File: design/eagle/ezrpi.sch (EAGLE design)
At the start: 40 parts

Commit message: unified cap value 100nF = 0.1uF
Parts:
- C9: value 100nF -> 0.1uF
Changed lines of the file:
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@@
 <part name="C7" library="passive" deviceset="CAP" device="0805" value="0.1uF"/>
 <part name="C8" library="passive" deviceset="CAP" device="0805" value="0.1uF"/>
-<part name="C9" library="passive" deviceset="CAP" device="0805" value="100nF"/>
+<part name="C9" library="passive" deviceset="CAP" device="0805" value="0.1uF"/>
 <part name="GND-ISO5" library="setup" deviceset="GND" device=""/>
 <part name="C10" library="passive" deviceset="CAP" device="0805" value="0.1uF"/>

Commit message: added top ground plane, fixed silk & naming
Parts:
- removed U$3: JTAG-6PINS, setup:JTAG-6PINS
- removed U$4: 26MHz, xtal:ABM8
- added SMA: (no value), connector:SMACONNECTOR
- added SWD: FTSH2X5, connector:FTSH2X5
- X1: value (none) -> 26MHz; device connector:SMACONNECTOR -> xtal:ABM8
- renumbered U$1 to MCU, U$2 to RPI, U$5 to X3, U$6 to X2
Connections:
- net GND: now also SMA.GND1, SMA.GND2, SMA.GND3, SMA.GND4, SWD.GND@1, SWD.GND@2, SWD.GND@3, X1.GND@2, X1.GND@4; no longer U$3.GND, U$4.GND@2, U$4.GND@4, X1.GND1, X1.GND2, X1.GND3, X1.GND4
- net N$1: now also SMA.ANT; no longer X1.ANT
- net RESET: now also SWD.RESET; no longer U$3.RESET
- net SWCLK: now also SWD.SWCLK; no longer U$3.SWCLK
- net SWDIO: now also SWD.SWDIO; no longer U$3.SWDIO
- net SWO: now also SWD.SWO; no longer U$3.SWO
- net VCC: now also SWD.VCC; no longer U$3.VCC
- net XIN: now also X1.1; no longer U$4.1
- net XOUT: now also X1.3; no longer U$4.3

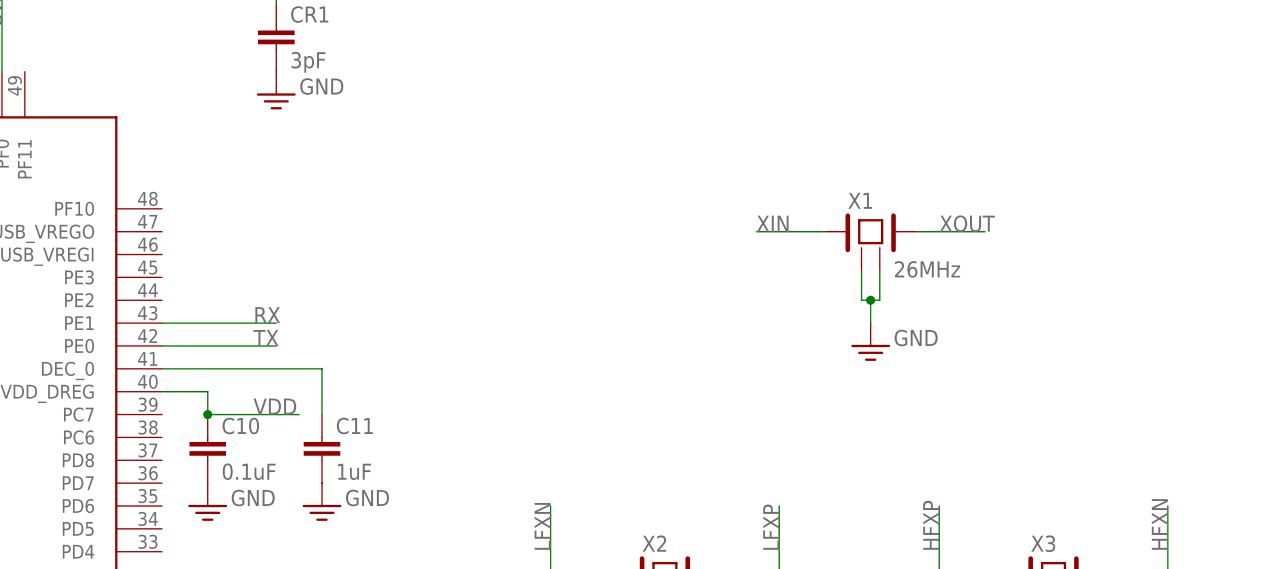
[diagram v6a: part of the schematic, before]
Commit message: added LEDs, improved traces, 50 Ω line, added vias
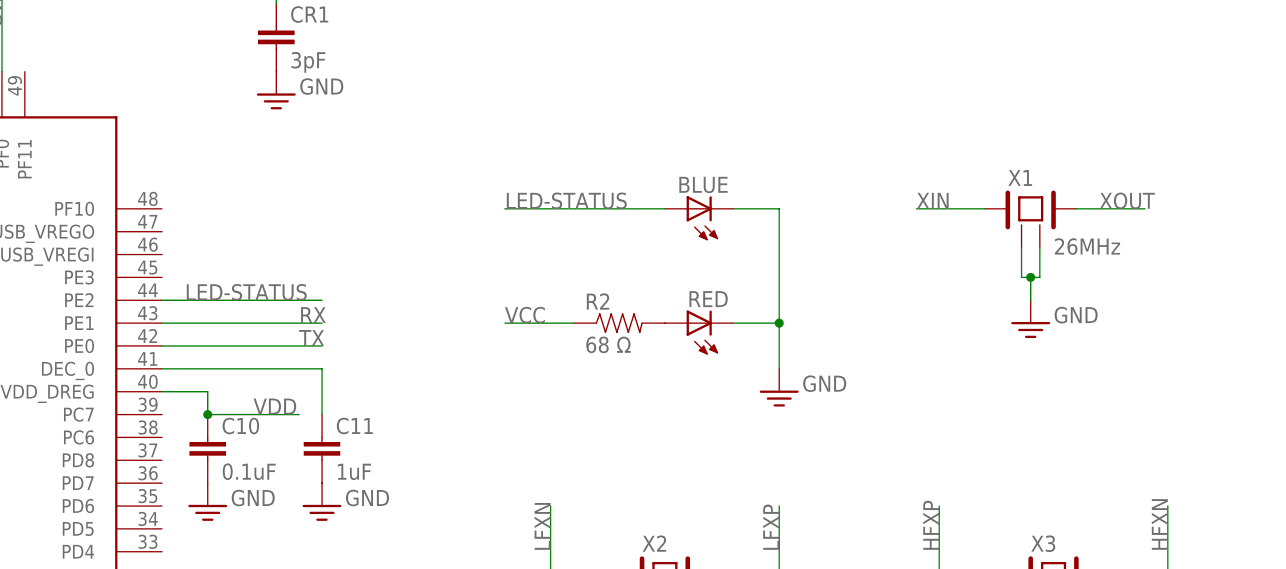
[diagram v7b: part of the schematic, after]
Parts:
- added BLUE, RED: (no value), led:LEDCHIPLED_0805
- added R2: 68 Ω, passive:RESISTOR0805-RES
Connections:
- new net LED-STATUS: BLUE.A, MCU.PE2
- new net N$8: R2.2, RED.A
- net GND: now also BLUE.C, RED.C
- net VCC: now also R2.1
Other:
- moved on the sheet: X1
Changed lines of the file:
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@@
 <part name="C0" library="passive" deviceset="CAP" device="0805" value="1uF"/>
 <part name="SWD" library="connector" deviceset="FTSH2X5" device=""/>
+<part name="BLUE" library="led" deviceset="LED" device="CHIPLED_0805"/>
+<part name="RED" library="led" deviceset="LED" device="CHIPLED_0805"/>
+<part name="R2" library="passive" deviceset="RESISTOR" device="0805-RES" value="68 Ω"/>
+<part name="GND" library="setup" deviceset="GND" device=""/>
 </parts>
 <sheets>
@@
 <instance part="GND-ISO17" gate="G$1" x="251.46" y="-43.18"/>
 <instance part="GND-ISO18" gate="G$1" x="276.86" y="-43.18"/>
-<instance part="GND-ISO20" gate="G$1" x="243.84" y="-5.08"/>
-<instance part="X1" gate="G$1" x="243.84" y="7.62"/>
+<instance part="GND-ISO20" gate="G$1" x="261.62" y="-2.54"/>
+<instance part="X1" gate="G$1" x="261.62" y="10.16"/>
 <instance part="X3" gate="G$1" x="264.16" y="-30.48"/>
 <instance part="X2" gate="G$1" x="220.98" y="-30.48"/>
@@
 <instance part="C0" gate="G$1" x="190.5" y="60.96" rot="R90"/>
 <instance part="SWD" gate="G$1" x="111.76" y="66.04"/>
+<instance part="BLUE" gate="G$1" x="223.52" y="10.16" rot="R90"/>
+<instance part="RED" gate="G$1" x="223.52" y="-2.54" rot="R90"/>
+<instance part="R2" gate="G$1" x="215.9" y="-2.54"/>
+<instance part="GND" gate="G$1" x="233.68" y="-10.16"/>
 </instances>
 <busses>
@@
 <pinref part="SUPPLY7" gate="G$1" pin="VCC"/>
 <pinref part="LCHOKE" gate="G$1" pin="1"/>
+</segment>
+<segment>
+<pinref part="R2" gate="G$1" pin="1"/>
+<wire x1="210.82" y1="-2.54" x2="203.2" y2="-2.54" width="0.1524" layer="91"/>
+<label x="203.2" y="-2.54" size="1.778" layer="95"/>
 </segment>
 </net>
@@
 <segment>
 <pinref part="GND-ISO20" gate="G$1" pin="GND-ISO"/>
-<wire x1="243.84" y1="-2.54" x2="243.84" y2="0" width="0.1524" layer="91"/>
+<wire x1="261.62" y1="0" x2="261.62" y2="2.54" width="0.1524" layer="91"/>
 <pinref part="X1" gate="G$1" pin="GND@2"/>
-<wire x1="243.84" y1="0" x2="244.856" y2="0" width="0.1524" layer="91"/>
-<wire x1="244.856" y1="0" x2="244.856" y2="3.302" width="0.1524" layer="91"/>
+<wire x1="261.62" y1="2.54" x2="262.636" y2="2.54" width="0.1524" layer="91"/>
+<wire x1="262.636" y1="2.54" x2="262.636" y2="5.842" width="0.1524" layer="91"/>
 <pinref part="X1" gate="G$1" pin="GND@4"/>
-<wire x1="243.84" y1="0" x2="242.824" y2="0" width="0.1524" layer="91"/>
-<wire x1="242.824" y1="0" x2="242.824" y2="3.302" width="0.1524" layer="91"/>
-<junction x="243.84" y="0"/>
+<wire x1="261.62" y1="2.54" x2="260.604" y2="2.54" width="0.1524" layer="91"/>
+<wire x1="260.604" y1="2.54" x2="260.604" y2="5.842" width="0.1524" layer="91"/>
+<junction x="261.62" y="2.54"/>
 </segment>
 <segment>
@@
 <pinref part="GND-ISO26" gate="G$1" pin="GND-ISO"/>
 </segment>
+<segment>
+<pinref part="RED" gate="G$1" pin="C"/>
+<pinref part="GND" gate="G$1" pin="GND-ISO"/>
+<wire x1="228.6" y1="-2.54" x2="233.68" y2="-2.54" width="0.1524" layer="91"/>
+<wire x1="233.68" y1="-2.54" x2="233.68" y2="-7.62" width="0.1524" layer="91"/>
+<pinref part="BLUE" gate="G$1" pin="C"/>
+<wire x1="228.6" y1="10.16" x2="233.68" y2="10.16" width="0.1524" layer="91"/>
+<wire x1="233.68" y1="10.16" x2="233.68" y2="-2.54" width="0.1524" layer="91"/>
+<junction x="233.68" y="-2.54"/>
+</segment>
 </net>
 <net name="RESET" class="0">
@@
 <net name="XIN" class="0">
 <segment>
-<wire x1="238.76" y1="7.62" x2="231.14" y2="7.62" width="0.1524" layer="91"/>
-<label x="231.14" y="7.62" size="1.778" layer="95"/>
+<wire x1="256.54" y1="10.16" x2="248.92" y2="10.16" width="0.1524" layer="91"/>
+<label x="248.92" y="10.16" size="1.778" layer="95"/>
 <pinref part="X1" gate="G$1" pin="1"/>
 </segment>
@@
 <net name="XOUT" class="0">
 <segment>
-<wire x1="248.92" y1="7.62" x2="256.54" y2="7.62" width="0.1524" layer="91"/>
-<label x="251.46" y="7.62" size="1.778" layer="95"/>
+<wire x1="266.7" y1="10.16" x2="274.32" y2="10.16" width="0.1524" layer="91"/>
+<label x="269.24" y="10.16" size="1.778" layer="95"/>
 <pinref part="X1" gate="G$1" pin="3"/>
 </segment>
@@
 <segment>
 <pinref part="MCU" gate="G$1" pin="PE1"/>
-<wire x1="165.1" y1="-2.54" x2="177.8" y2="-2.54" width="0.1524" layer="91"/>
-<label x="175.26" y="-2.54" size="1.778" layer="95"/>
+<wire x1="165.1" y1="-2.54" x2="182.88" y2="-2.54" width="0.1524" layer="91"/>
+<label x="180.34" y="-2.54" size="1.778" layer="95"/>
 </segment>
 </net>
@@
 <segment>
 <pinref part="MCU" gate="G$1" pin="PE0"/>
-<wire x1="165.1" y1="-5.08" x2="177.8" y2="-5.08" width="0.1524" layer="91"/>
-<label x="175.26" y="-5.08" size="1.778" layer="95"/>
-</segment>
-</net>
+<wire x1="165.1" y1="-5.08" x2="182.88" y2="-5.08" width="0.1524" layer="91"/>
+<label x="180.34" y="-5.08" size="1.778" layer="95"/>
+</segment>
+</net>
+<net name="LED-STATUS" class="0">
+<segment>
+<pinref part="MCU" gate="G$1" pin="PE2"/>
+<wire x1="165.1" y1="0" x2="182.88" y2="0" width="0.1524" layer="91"/>
+<label x="167.64" y="0" size="1.778" layer="95"/>
+</segment>
+<segment>
+<pinref part="BLUE" gate="G$1" pin="A"/>
+<wire x1="220.98" y1="10.16" x2="203.2" y2="10.16" width="0.1524" layer="91"/>
+<label x="203.2" y="10.16" size="1.778" layer="95"/>
+</segment>
+</net>
+<net name="N$8" class="0">
+<segment>
+<pinref part="R2" gate="G$1" pin="2"/>
+<pinref part="RED" gate="G$1" pin="A"/>
+</segment>
+</net>
